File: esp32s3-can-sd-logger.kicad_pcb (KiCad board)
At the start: 4 copper layers, 84 x 84 mm, 179 parts, among them J1 PWR + CAN harness, J10 Sensor harness, J2 USB-C, J3 UART0, J4 I2C / Qwiic, J5 SPI, J6 WS2812, J7 Spare IO, J8 Rail break-out, J9 microSD push-pull, Q1 100V 6.8mOhm N-ch, Q2 -20V 2.3A P-ch, Q3 60V 300mA N-ch, SW1 RESET, SW2 BOOT, U1 LM74700-Q1, U2 LM5164 (5V), U3 LM5164 (3V3), U4 ESP32-S3-WROOM-1-N16R8, U5 USBLC6-2SC6, U6 74AHCT1G125, U7 TJA1051T/3, U8 ADS1115

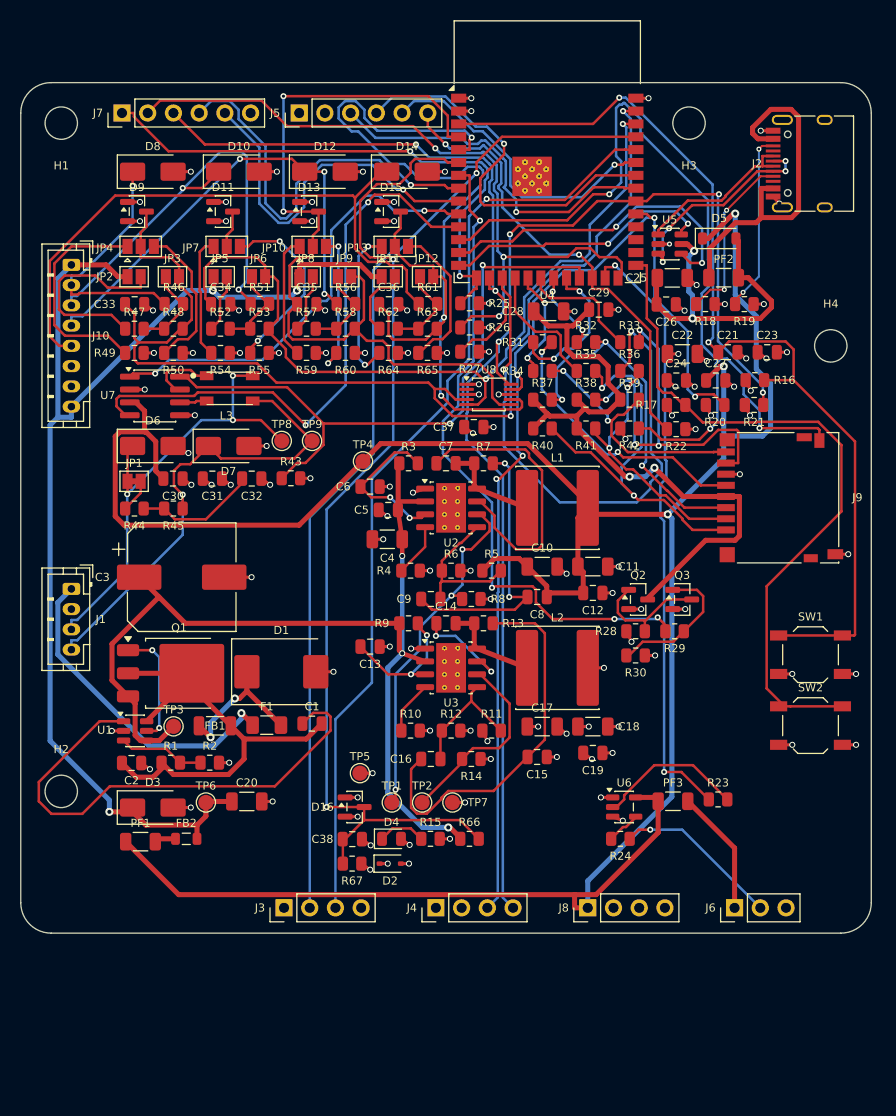
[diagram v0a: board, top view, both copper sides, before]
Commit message: Board: corner mounting holes, USB at the edge, and room for the silkscreen
Five placement changes, all from Matt looking at the render:

  - U2, U3 and L3 were invisible. The bucks' footprint names an exposed-pad
    variant KiCad ships no model for, and the CAN choke is a project
    footprint with no model at all. Both now borrow one from the same class
    of part -- the 2.41x3.81 SOIC-8-1EP and an 1812 inductor, the choke's
    body being 4.5 x 3.2 mm. An audit of all 36 footprints says the only
    others without models are the solder jumpers, mounting holes and test
    points, which have no body to draw.

  - The zone packer now shares a zone's unused height between its rows. The
    analogue channels were packing 20.7 mm of parts into a 28 mm shelf and
    then sitting them 0.4 mm apart, which is why the reference designators
    ran together. The whole left column shifts down to pay for it: the CAN
    block with U7 and L3, then the battery front end, then the sensor-5V
    group. Silkscreen the tidier could not place fell from 39 to 6.

  - H3 and H4 move to the top-right and bottom-right corners. They were
    inboard -- H3 beside the module, H4 halfway down the right edge -- which
    put fixings where the USB port and the MCU passives wanted to be. H4
    sits at y=72, not 76: at 76 an M3 screw head would have fouled J6.

  - J2 drops from y=8 to y=16, clear of the corner hole and above J9, and
    the MCU passives spread into the space H4 left.

  - J2's shell face moves from 2 mm inside the outline to 0.5 mm. Two
    millimetres of laminate in front of the mouth is enough to stop a plug's
    overmould seating; 0.5 mm is as close as the body can go and still be
    inside the board for assembly.

Rerouted from scratch: 0 DRC errors, 0 unconnected. Remaining 36 DRC
warnings are all silkscreen. Schematic and netlist untouched; fab/ and
plots/ regenerated.

Co-Authored-By: Claude Opus 5 <noreply@anthropic.com>
Claude-Session: https://claude.ai/code/sessi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
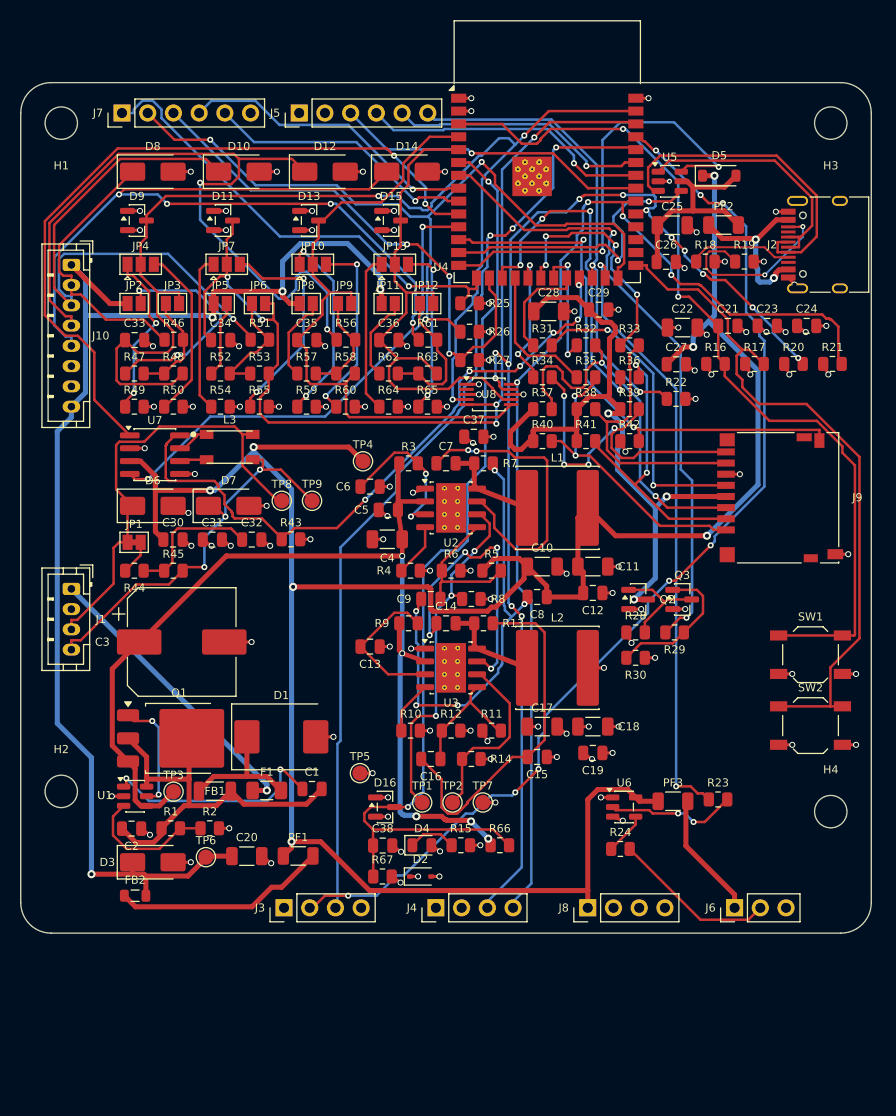
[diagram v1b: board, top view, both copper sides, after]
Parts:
- moved H4 46.0 mm to (80.0, 72.0)
- moved PF1 15.6 mm to (27.4, 76.4)
- moved H3 14.0 mm to (80.0, 4.00)
- moved C24 14.0 mm to (77.6, 24.0)
- moved R17 8.74 mm to (72.5, 27.8)
- moved R21 8.74 mm to (80.2, 27.8)
- moved R20 8.74 mm to (76.3, 27.8)
- moved J2 8.14 mm to (79.8, 16.0)
- moved FB2 7.56 mm to (11.3, 80.3)
- moved C2 6.48 mm to (10.9, 73.7)
- moved R1 6.48 mm to (14.8, 73.6)
- moved R2 6.48 mm to (18.7, 73.6)
- moved TP3 6.45 mm to (15.1, 70.0)
- moved C1 6.45 mm to (28.8, 69.8)
- moved FB1 6.45 mm to (19.2, 70.0)
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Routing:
- net AIN4: track 95.3 -> 52.1 mm, vias 3 -> 0
- net SD_CD: track 88.2 -> 53.9 mm, vias 3 -> 2
- net +5V: track 262.5 -> 233.4 mm, vias 3 -> 7
- net CAN_TX: track 44.4 -> 72.8 mm
- net VCAP: track 50.2 -> 22.4 mm, vias 0 -> 2
- net AIN3_IN: track 46.6 -> 73.3 mm, vias 3 -> 2
- net AIN4_IN: track 61.9 -> 85.0 mm, vias 0 -> 4
- net SD_D3: track 56.4 -> 33.9 mm, vias 2 -> 4
- net VSENS_F: track 2.11 -> 21.2 mm
- net AIN3: track 84.1 -> 65.2 mm, vias 2 -> 0
- net BST_3V3: track 10.0 -> 28.8 mm, vias 2 -> 4
- net VBUS_IN: track 35.0 -> 16.3 mm, vias 0 -> 2
- net USB_DP: track 26.7 -> 43.8 mm
- net AIN2: track 84.7 -> 100.3 mm, vias 2 -> 5
- net RAMP_5V: track 27.8 -> 42.4 mm, vias 2 -> 5
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
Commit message: Board: put the four mounting holes on a square
They were at three different insets -- a fixing beside the module, another
halfway down the right edge, and the bottom pair 6 mm out of line with the
top, left over from when the board was 74 mm tall. Now one per corner, 4 mm
in from each, so the four of them form a 76 x 76 square.

4 mm rather than something rounder is set by H1: the keepout ring is 6.94 mm
across, and any further in it eats into J7, which cannot move because the
top header row has no slack. At the other end J6 shifts 1.5 mm left so H4's
ring clears the connector body by 1.7 mm -- at the old position the screw
head would have overlapped its corner.

Rerouted: 0 DRC errors, 0 unconnected, 36 silkscreen warnings. Schematic
and netlist untouched; fab/ and plots/ regenerated.

Co-Authored-By: Claude Opus 5 <noreply@anthropic.com>
Claude-Session: https://claude.ai/code/session_01DhNbL25h25p8VFCjRfJik9
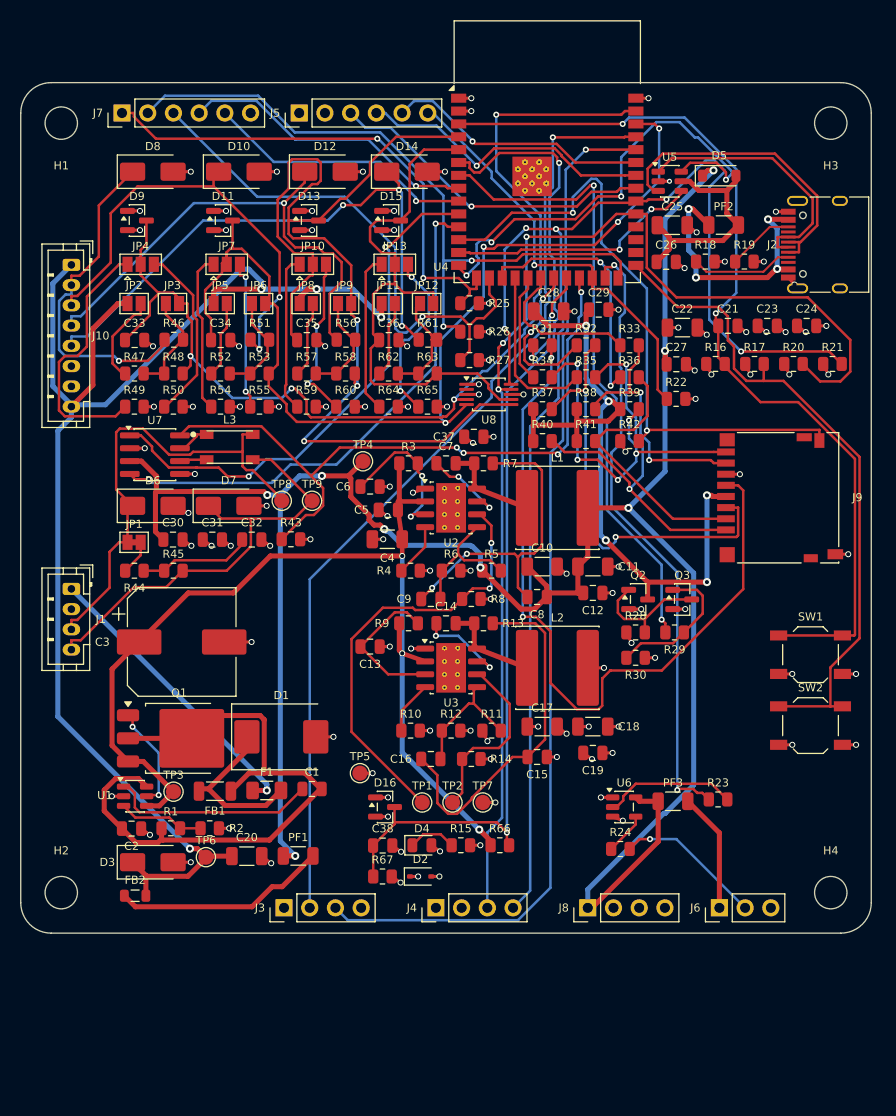
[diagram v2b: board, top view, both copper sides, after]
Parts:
- moved H2 10.0 mm to (4.00, 80.0)
- moved H4 8.00 mm to (80.0, 80.0)
- moved J6 1.50 mm to (69.0, 81.5)
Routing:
- net SD_CLK_C: track 30.7 -> 74.7 mm
- net AIN3: track 65.2 -> 105.2 mm, vias 0 -> 3
- net I2C_SCL: track 107.5 -> 139.1 mm, vias 4 -> 5
- net AIN4_IN: track 85.0 -> 57.4 mm, vias 4 -> 3
- net AIN3_IN: track 73.3 -> 49.0 mm, vias 2 -> 1
- net VBAT_FB: track 40.4 -> 63.2 mm
- net BST_5V: track 29.8 -> 8.53 mm
- net CAN_TX: track 72.8 -> 52.5 mm
- net BST_3V3: track 28.8 -> 9.36 mm, vias 4 -> 2
- net +5V: track 233.4 -> 218.7 mm, vias 7 -> 8
- net AIN1_PU: track 22.5 -> 9.08 mm, vias 2 -> 0
- net AIN1: track 118.3 -> 105.6 mm, vias 3 -> 4
- net USB_CC2: track 18.6 -> 6.67 mm, vias 2 -> 0
- net +5VS: track 130.4 -> 141.9 mm
- net AIN2_IN: track 56.4 -> 44.9 mm, vias 1 -> 2
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
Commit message: Power-fail ride-through: detect, coast, shed; board grows to 84 x 100
The ignition cuts this board's power with a log file open, every drive.
Three new pieces make that survivable, all simulated before layout:

- Detect: TLV431 + 100k/12.7k divider on VBAT_F, AHEAD of the ideal
  diode, asserting PWR_FAIL (IO15) at 11.0 V with ~0.3 V hysteresis.
  The harness collapses microseconds after the key turns while +VBAT
  coasts, so the warning costs no stored energy.
- Coast: two 220 uF/100 V cans join the 100 uF on +VBAT. 540 uF on the
  input rail, where a volt of headroom is worth most.
- Shed: AO3401 + 2N7002 high-side switch on the sensor rail (SENS_EN,
  IO16, off at reset), with PF1 moved behind it so a tripped sensor
  fuse can also be power-cycled from firmware.

Simulated end to end: detection <1 ms after the cut, then 108 ms to
converter dropout with sensors shed, 53 ms without -- the switch doubles
the flush budget. ISO pulse 1's brownout shortens from 8.2 to 5.6 ms.

The two cans plus the detector had no free board left on 84 x 84, so the
board grows to 84 x 100 (still JLC's cheap tier): bottom-edge furniture
and mounting holes move down 16 mm, one can per side, and the detector/
switch column gets its own placement zone. Also included from the audit:
the 3V3 buck's own input capacitor pair at its VIN pin (it was reaching
12.6 mm across to the 5 V island's), the CAN transceiver and AHCT buffer
bypasses pinned at their pins, and Power-class tracks at 0.55 mm to clear
IPC-2221 for 2 A at a 20 C rise.

Hard-won generator fix: a literal newline inside a symbol property is
accepted by KiCad's loader but silently breaks connectivity for every
symbol after it in the file -- the netlist dropped 45 components with no
error pointing anywhere near the cause. The emitter now flattens all
whitespace in property strings.

Board: 0 DRC violations, 0 unconnected, physical audit clean end to end.
185 components, 111 nets, ERC clean, netlist verified node-for-node.

Co-Authore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
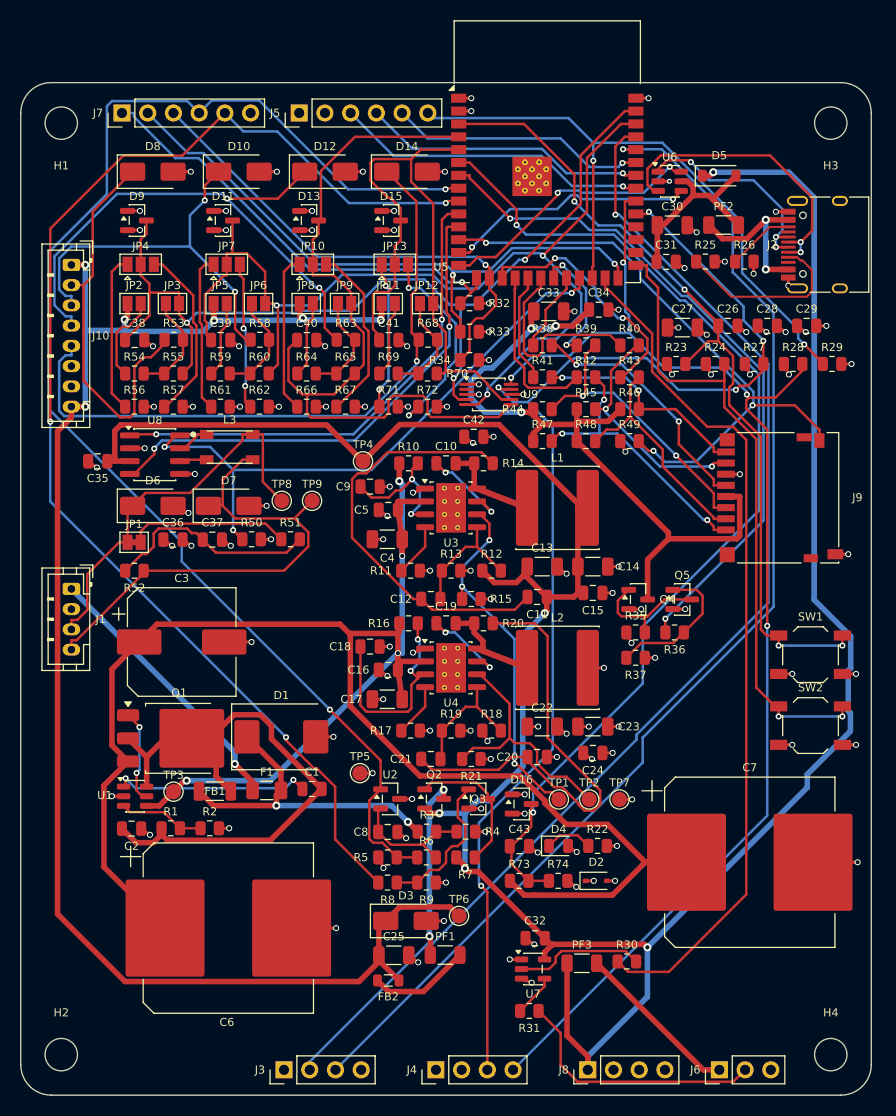
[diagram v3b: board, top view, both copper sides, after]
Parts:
- added C39: 100nF, C_0805_2012Metric, F.Cu at (19.7, 25.4)
- added C40: 100nF, C_0805_2012Metric, F.Cu at (28.2, 25.4)
- added C41: 100nF, C_0805_2012Metric, F.Cu at (36.3, 25.4)
- added C42: 100nF, C_0805_2012Metric, F.Cu at (44.7, 35.0)
- added C43: 100nF, C_0805_2012Metric, F.Cu at (49.2, 75.4)
- added Q4: -20V 2.3A P-ch, SOT-23, F.Cu at (61.0, 51.0)
- added Q5: 60V 300mA N-ch, SOT-23, F.Cu at (65.3, 51.0)
- added R68: 1k, R_0805_2012Metric, F.Cu at (40.2, 25.4)
- added R69: 2.49k, R_0805_2012Metric, F.Cu at (36.3, 28.7)
- added R70: 10k, R_0805_2012Metric, F.Cu at (40.2, 28.7)
- added R71: 15k, R_0805_2012Metric, F.Cu at (36.3, 32.0)
- added R72: 2.21k, R_0805_2012Metric, F.Cu at (40.2, 32.0)
- added R73: 100k, R_0805_2012Metric, F.Cu at (49.2, 78.8)
- added R74: 8.2k, R_0805_2012Metric, F.Cu at (53.1, 78.8)
- added U9: ADS1115, VSSOP-10_3x3mm_P0.5mm, F.Cu at (46.2, 30.8)
- C10: value 22uF -> 2.2nF; footprint C_1206_3216Metric -> C_0805_2012Metric
- C11: value 22uF -> 3.3nF; footprint C_1206_3216Metric -> C_0805_2012Metric
- C12: value 100nF -> 270pF
- C13: value 10nF -> 22uF; footprint C_0805_2012Metric -> C_1206_3216Metric
- C14: value 2.2nF -> 22uF; footprint C_0805_2012Metric -> C_1206_3216Metric
- C15: value 3.3nF -> 100nF
- C16: value 270pF -> 100nF
- C17: value 22uF -> 10uF
- C18: value 22uF -> 10nF; footprint C_1206_3216Metric -> C_0805_2012Metric
- C19: value 100nF -> 2.2nF
- C20: value 10uF -> 3.3nF; footprint C_1206_3216Metric -> C_0805_2012Metric
- C21: value 1uF -> 270pF
- C22: value 10uF -> 22uF
- C23: value 100nF -> 22uF; footprint C_0805_2012Metric -> C_1206_3216Metric
- C26: value 100nF -> 1uF
- C27, C30, C33: value 100nF -> 10uF; footprint C_0805_2012Metric -> C_1206_3216Metric
- C28: value 10uF -> 100nF; footprint C_1206_3216Metric -> C_0805_2012Metric
- C32: value 4.7nF -> 100nF
- C37: value 100nF -> 4.7nF
- C6: value 10nF -> 220uF; footprint C_0805_2012Metric -> CP_Elec_16x17.5
- C7: value 2.2nF -> 220uF; footprint C_0805_2012Metric -> CP_Elec_16x17.5
- C8: value 3.3nF -> 1nF
- C9: value 270pF -> 10nF
- Q2: value -20V 2.3A P-ch -> P-ch 30V 3A
- Q3: value 60V 300mA N-ch -> N-ch 60V 200mA
- R10: value 20.5k -> 100k
- R11: value 100k -> 31.6k
- R12: value 57.6k -> 100k
- R13: value 95.3k -> 31.6k
- R14: value 100k -> 121k
- R15: value 1k -> 100k
- R16, R37: value 10k -> 100k
- R17: value 10k -> 20.5k
- R18: value 5.1k -> 100k
- R19: value 5.1k -> 57.6k
- R20: value 4.7k -> 95.3k
- R21: value 4.7k -> 100k
- R22, R53, R58, R63: value 10k -> 1k
- R23, R32, R33, R34: value 33 -> 10k
- R24: value 100 -> 10k
- R25, R26: value 10k -> 5.1k
- R27: value 10k -> 4.7k
- R28: value 100k -> 4.7k
- R29, R46: value 1k -> 10k
- R30: value 100k -> 33
- R31: value 33 -> 100
- R35: value 33 -> 100k
- R36: value 33 -> 1k
- R38, R39, R40, R41, R43: value 10k -> 33
- R4: value 31.6k -> 12.7k
- R42: value 47k -> 33
- R44, R45: value 60.4 -> 10k
- R47: value 2.49k -> 10k
- R49: value 15k -> 47k
- R5, R8: value 100k -> 10k
- R50, R55, R60, R65: value 2.21k -> 10k
- R51: value 1k -> 60.4
- R52: value 2.49k -> 60.4
- R54, R59, R64: value 15k -> 2.49k
- R56, R61: value 1k -> 15k
- R57, R62: value 2.49k -> 2.21k
- R6: value 31.6k -> 1M
- R66: value 100k -> 15k
- R67: value 8.2k -> 2.21k
- R7: value 121k -> 100k
- U2: value LM5164 (5V) -> TLV431A; footprint SOIC-8-1EP_3.9x4.9mm_P1.27mm_EP2.95x4.9mm_Mask2.71x3.4mm_ThermalVias -> SOT-23
- U3: value LM5164 (3V3) -> LM5164 (5V)
- U4: value ESP32-S3-WROOM-1-N16R8 -> LM5164 (3V3); footprint ESP32-S3-WROOM-1 -> SOIC-8-1EP_3.9x4.9mm_P1.27mm_EP2.95x4.9mm_Mask2.71x3.4mm_ThermalVias
- U5: value USBLC6-2SC6 -> ESP32-S3-WROOM-1-N16R8; footprint SOT-23-6 -> ESP32-S3-WROOM-1
- U6: value 74AHCT1G125 -> USBLC6-2SC6; footprint SOT-23-5 -> SOT-23-6
- U7: value TJA1051T/3 -> 74AHCT1G125; footprint SOIC-8_3.9x4.9mm_P1.27mm -> SOT-23-5
- U8: value ADS1115 -> TJA1051T/3; footprint VSSOP-10_3x3mm_P0.5mm -> SOIC-8_3.9x4.9mm_P1.27mm
- moved C25 77.2 mm to (36.8, 86.2)
- moved R31 65.8 mm to (50.2, 91.7)
- moved U7 63.1 mm to (50.6, 87.5)
- moved U6 62.0 mm to (64.1, 9.74)
- moved C30 58.3 mm to (64.3, 14.1)
- moved C38 55.6 mm to (11.2, 25.4)
- moved R19 54.6 mm to (42.5, 64.0)
- moved R21 52.9 mm to (44.5, 66.8)
- moved C31 52.5 mm to (63.7, 17.7)
- moved U4 51.9 mm to (42.5, 57.8)
- moved C21 51.9 mm to (40.5, 66.8)
- moved R18 50.9 mm to (46.5, 64.0)
- moved R17 49.7 mm to (38.5, 64.0)
- moved C7 49.5 mm to (72.0, 77.0)
- moved R49 49.0 mm to (60.1, 35.4)
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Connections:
- C10 pad 1: +5V -> BST_5V
- C10 pad 2: GND -> SW_5V
- C11 pad 1: +5V -> RAMP_5V
- C11 pad 2: GND -> +5V
- C12 pad 1: +5V -> RAMP_5V
- C12 pad 2: GND -> FB_5V
- C13 pad 1: EN_3V3 -> +5V
- C14 pad 1: BST_3V3 -> +5V
- C14 pad 2: SW_3V3 -> GND
- C15 pad 1: RAMP_3V3 -> +5V
- C15 pad 2: +3V3 -> GND
- C16 pad 1: RAMP_3V3 -> +VBAT
- C16 pad 2: FB_3V3 -> GND
- C17 pad 1: +3V3 -> +VBAT
- C18 pad 1: +3V3 -> EN_3V3
- C19 pad 1: +3V3 -> BST_3V3
- C19 pad 2: GND -> SW_3V3
- C20 pad 1: +5VS -> RAMP_3V3
- C20 pad 2: GND -> +3V3
- C21 pad 1: MCU_EN -> RAMP_3V3
- C21 pad 2: GND -> FB_3V3
- C25 pad 1: VBUS -> +5VS
- C26 pad 1: VBUS -> MCU_EN
- C27 pad 1: +5V -> +3V3
- C28 pad 1: SD_VDD -> +3V3
- C29 pad 1: SD_VDD -> +3V3
- C30 pad 1: +5V -> VBUS
- C31 pad 1: +3V3 -> VBUS
- C32 pad 1: CAN_SPLIT -> +5V
- C33 pad 1: AIN1 -> SD_VDD
- C34 pad 1: AIN2 -> SD_VDD
- C35 pad 1: AIN3 -> +5V
- C36 pad 1: AIN4 -> +3V3
- C37 pad 1: +3V3 -> CAN_SPLIT
- C38 pad 1: VBAT_SNS -> AIN1
- C6 pad 1: EN_5V -> +VBAT
- C7 pad 1: BST_5V -> +VBAT
- C7 pad 2: SW_5V -> GND
- C8 pad 1: RAMP_5V -> PFD_SENSE
- C8 pad 2: +5V -> GND
- C9 pad 1: RAMP_5V -> EN_5V
- C9 pad 2: FB_5V -> GND
- J7 pad 4: IO15 -> PWR_FAIL
- J7 pad 5: IO16 -> SENS_EN
- PF1 pad 1: +5V -> VSENS_SW
- Q2 pad 1: SD_PG -> SENS_G
- Q2 pad 2: +3V3 -> +5V
- Q2 pad 3: SD_VDD -> VSENS_SW
- Q3 pad 1: SD_EN_G -> SENS_EN_G
- Q3 pad 3: SD_PG -> SENS_G
- R10 pad 1: RON_3V3 -> +VBAT
- R10 pad 2: GND -> EN_5V
- R11 pad 1: +3V3 -> RON_5V
- R11 pad 2: FB_3V3 -> GND
- R12 pad 1: FB_3V3 -> +5V
- R12 pad 2: GND -> FB_5V
- R13 pad 1: SW_3V3 -> FB_5V
- R13 pad 2: RAMP_3V3 -> GND
- R14 pad 1: PG_3V3 -> SW_5V
- R14 pad 2: +3V3 -> RAMP_5V
- R15 pad 1: PWR_LED_K -> PG_5V
- R15 pad 2: GND -> +3V3
- R16 pad 1: +3V3 -> +VBAT
- R16 pad 2: MCU_EN -> EN_3V3
- R17 pad 1: +3V3 -> RON_3V3
- R17 pad 2: MCU_BOOT -> GND
- R18 pad 1: USB_CC1 -> +3V3
- R18 pad 2: GND -> FB_3V3
- R19 pad 1: USB_CC2 -> FB_3V3
- R20 pad 1: +3V3 -> SW_3V3
- R20 pad 2: I2C_SDA -> RAMP_3V3
- R21 pad 1: +3V3 -> PG_3V3
- R21 pad 2: I2C_SCL -> +3V3
- R22 pad 1: SPI_CS -> PWR_LED_K
- R22 pad 2: +3V3 -> GND
- R23 pad 1: LED_DIN_MCU -> +3V3
- R23 pad 2: LED_DIN_A -> MCU_EN
- R24 pad 1: LED_DIN -> +3V3
- R24 pad 2: LED_DIN_J -> MCU_BOOT
- R25 pad 1: IO3 -> USB_CC1
- R26 pad 1: IO45 -> USB_CC2
- R27 pad 1: IO46 -> +3V3
- R27 pad 2: GND -> I2C_SDA
- R28 pad 2: SD_PG -> I2C_SCL
- R29 pad 1: SD_PWR_EN -> SPI_CS
- R29 pad 2: SD_EN_G -> +3V3
- R3 pad 1: +VBAT -> VBAT_F
- R3 pad 2: EN_5V -> PFD_SENSE
- R30 pad 1: SD_EN_G -> LED_DIN_MCU
- R30 pad 2: GND -> LED_DIN_A
- R31 pad 1: SD_CLK -> LED_DIN
- R31 pad 2: SD_CLK_C -> LED_DIN_J
- R32 pad 1: SD_CMD -> IO3
- R32 pad 2: SD_CMD_C -> GND
- R33 pad 1: SD_D0 -> IO45
- R33 pad 2: SD_D0_C -> GND
- R34 pad 1: SD_D1 -> IO46
- R34 pad 2: SD_D1_C -> GND
- R35 pad 1: SD_D2 -> +3V3
- R35 pad 2: SD_D2_C -> SD_PG
- R36 pad 1: SD_D3 -> SD_PWR_EN
- R36 pad 2: SD_D3_C -> SD_EN_G
- R37 pad 1: SD_VDD -> SD_EN_G
- R37 pad 2: SD_CMD_C -> GND
- R38 pad 1: SD_VDD -> SD_CLK
- R38 pad 2: SD_D0_C -> SD_CLK_C
- R39 pad 1: SD_VDD -> SD_CMD
- R39 pad 2: SD_D1_C -> SD_CMD_C
- R4 pad 1: RON_5V -> PFD_SENSE
- R40 pad 1: SD_VDD -> SD_D0
- R40 pad 2: SD_D2_C -> SD_D0_C
- R41 pad 1: SD_VDD -> SD_D1
- R41 pad 2: SD_D3_C -> SD_D1_C
- R42 pad 1: +3V3 -> SD_D2
- R42 pad 2: SD_CD -> SD_D2_C
- R43 pad 1: CAN_S -> SD_D3
- R43 pad 2: GND -> SD_D3_C
- R44 pad 1: TERM_A -> SD_VDD
- R44 pad 2: CAN_SPLIT -> SD_CMD_C
- R45 pad 1: CAN_SPLIT -> SD_VDD
- R45 pad 2: CAN_L -> SD_D0_C
- R46 pad 1: AIN1_IN -> SD_VDD
- R46 pad 2: AIN1_A -> SD_D1_C
- R47 pad 1: AIN1_PU -> SD_VDD
- R47 pad 2: AIN1_A -> SD_D2_C
- R48 pad 1: AIN1_A -> SD_VDD
- R48 pad 2: AIN1 -> SD_D3_C
- R49 pad 1: AIN1_R1 -> +3V3
- R49 pad 2: GND -> SD_CD
- R5 pad 1: +5V -> +3V3
- R5 pad 2: FB_5V -> PWR_FAIL
- R50 pad 1: AIN1_R2 -> CAN_S
- R51 pad 1: AIN2_IN -> TERM_A
- R51 pad 2: AIN2_A -> CAN_SPLIT
- R52 pad 1: AIN2_PU -> CAN_SPLIT
- R52 pad 2: AIN2_A -> CAN_L
- R53 pad 1: AIN2_A -> AIN1_IN
- R53 pad 2: AIN2 -> AIN1_A
- R54 pad 1: AIN2_R1 -> AIN1_PU
- R54 pad 2: GND -> AIN1_A
- R55 pad 1: AIN2_R2 -> AIN1_A
- R55 pad 2: GND -> AIN1
- R56 pad 1: AIN3_IN -> AIN1_R1
- R56 pad 2: AIN3_A -> GND
- R57 pad 1: AIN3_PU -> AIN1_R2
- R57 pad 2: AIN3_A -> GND
- R58 pad 1: AIN3_A -> AIN2_IN
- R58 pad 2: AIN3 -> AIN2_A
- R59 pad 1: AIN3_R1 -> AIN2_PU
- R59 pad 2: GND -> AIN2_A
- R6 pad 1: FB_5V -> PWR_FAIL
- R6 pad 2: GND -> PFD_SENSE
- R60 pad 1: AIN3_R2 -> AIN2_A
- R60 pad 2: GND -> AIN2
- R61 pad 1: AIN4_IN -> AIN2_R1
- R61 pad 2: AIN4_A -> GND
- R62 pad 1: AIN4_PU -> AIN2_R2
- R62 pad 2: AIN4_A -> GND
- R63 pad 1: AIN4_A -> AIN3_IN
- R63 pad 2: AIN4 -> AIN3_A
- R64 pad 1: AIN4_R1 -> AIN3_PU
- R64 pad 2: GND -> AIN3_A
- R65 pad 1: AIN4_R2 -> AIN3_A
- R65 pad 2: GND -> AIN3
- R66 pad 1: +VBAT -> AIN3_R1
- R66 pad 2: VBAT_SNS -> GND
- R67 pad 1: VBAT_SNS -> AIN3_R2
- R7 pad 1: SW_5V -> +5V
- R7 pad 2: RAMP_5V -> SENS_G
- R8 pad 1: PG_5V -> SENS_EN
- R8 pad 2: +3V3 -> SENS_EN_G
- R9 pad 1: +VBAT -> SENS_EN_G
- R9 pad 2: EN_3V3 -> GND
- U2 pad 1: GND -> PWR_FAIL
- U2 pad 2: +VBAT -> PFD_SENSE
- U2 pad 3: EN_5V -> GND
- U3 pad 3: EN_3V3 -> EN_5V
- U3 pad 4: RON_3V3 -> RON_5V
- U3 pad 5: FB_3V3 -> FB_5V
- U3 pad 6: PG_3V3 -> PG_5V
- U3 pad 7: BST_3V3 -> BST_5V
- U3 pad 8: SW_3V3 -> SW_5V
- U4 pad 2: +3V3 -> +VBAT
- U4 pad 3: MCU_EN -> EN_3V3
- U4 pad 4: AIN3 -> RON_3V3
- U4 pad 5: AIN4 -> FB_3V3
- U4 pad 6: VBAT_SNS -> PG_3V3
- U4 pad 7: SD_PWR_EN -> BST_3V3
- U4 pad 8: IO15 -> SW_3V3
- U4 pad 9: IO16 -> GND
- U5 pad 1: USB_DP_CON -> GND
- U5 pad 2: GND -> +3V3
- U5 pad 3: USB_DM_CON -> MCU_EN
- U5 pad 4: USB_DM -> AIN3
- U5 pad 5: VBUS -> AIN4
- U5 pad 6: USB_DP -> VBAT_SNS
- U6 pad 1: GND -> USB_DP_CON
- U6 pad 2: LED_DIN_A -> GND
- U6 pad 3: GND -> USB_DM_CON
- U6 pad 4: LED_DIN -> USB_DM
- U6 pad 5: +5V -> VBUS
- U7 pad 1: CAN_TX -> GND
- U7 pad 2: GND -> LED_DIN_A
- U7 pad 3: +5V -> GND
- U7 pad 4: CAN_RX -> LED_DIN
- U7 pad 5: +3V3 -> +5V
- U8 pad 1: GND -> CAN_TX
- U8 pad 2: (no net) -> GND
- U8 pad 3: GND -> +5V
- U8 pad 4: AIN1 -> CAN_RX
- U8 pad 5: AIN2 -> +3V3
- U8 pad 6: AIN3 -> CANL_T
- U8 pad 7: AIN4 -> CANH_T
- U8 pad 8: +3V3 -> CAN_S
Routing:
- net PWR_FAIL: track 0.00 -> 134.0 mm, vias 0 -> 2
- net SENS_EN: track 0.00 -> 127.0 mm, vias 0 -> 3
- net +VBAT: track 101.6 -> 191.9 mm, vias 3 -> 4
- net SD_CLK_C: track 74.7 -> 24.6 mm
- net +5V: track 218.7 -> 261.6 mm, vias 8 -> 5
- net IO15: track 29.7 -> 0.00 mm, vias 1 -> 0
- net AIN3: track 105.2 -> 77.3 mm, vias 3 -> 0
- net IO16: track 26.9 -> 0.00 mm, vias 1 -> 0
- net UART_TX: track 94.6 -> 119.1 mm
- net SPI_CS: track 42.4 -> 66.2 mm, vias 1 -> 2
- net LED_DIN_MCU: track 61.3 -> 84.6 mm, vias 2 -> 0
- net USB_DP: track 46.6 -> 26.5 mm, vias 4 -> 2
- net VSENS_SW: track 0.00 -> 17.8 mm, vias 0 -> 2
- net GND: track 108.6 -> 125.0 mm, vias 88 -> 97
- net UART_RX: track 102.5 -> 118.5 mm
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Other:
- board size 84 x 84 mm -> 84 x 100 mm
